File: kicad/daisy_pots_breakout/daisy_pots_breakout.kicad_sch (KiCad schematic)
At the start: 6 parts, among them J1 Conn_01x11_Pin, SW1 RotaryEncoder_Switch

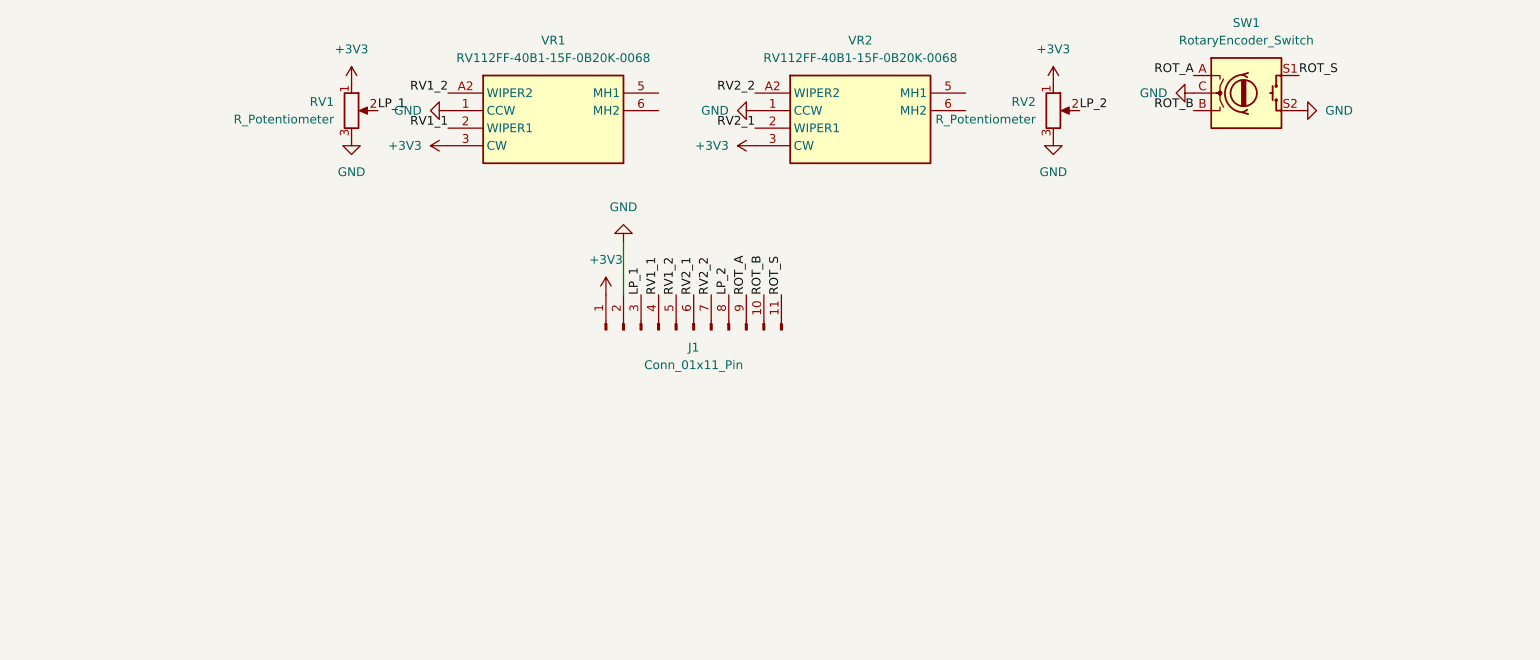
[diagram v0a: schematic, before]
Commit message: Make side boards for pots and buttons use same connector as main board
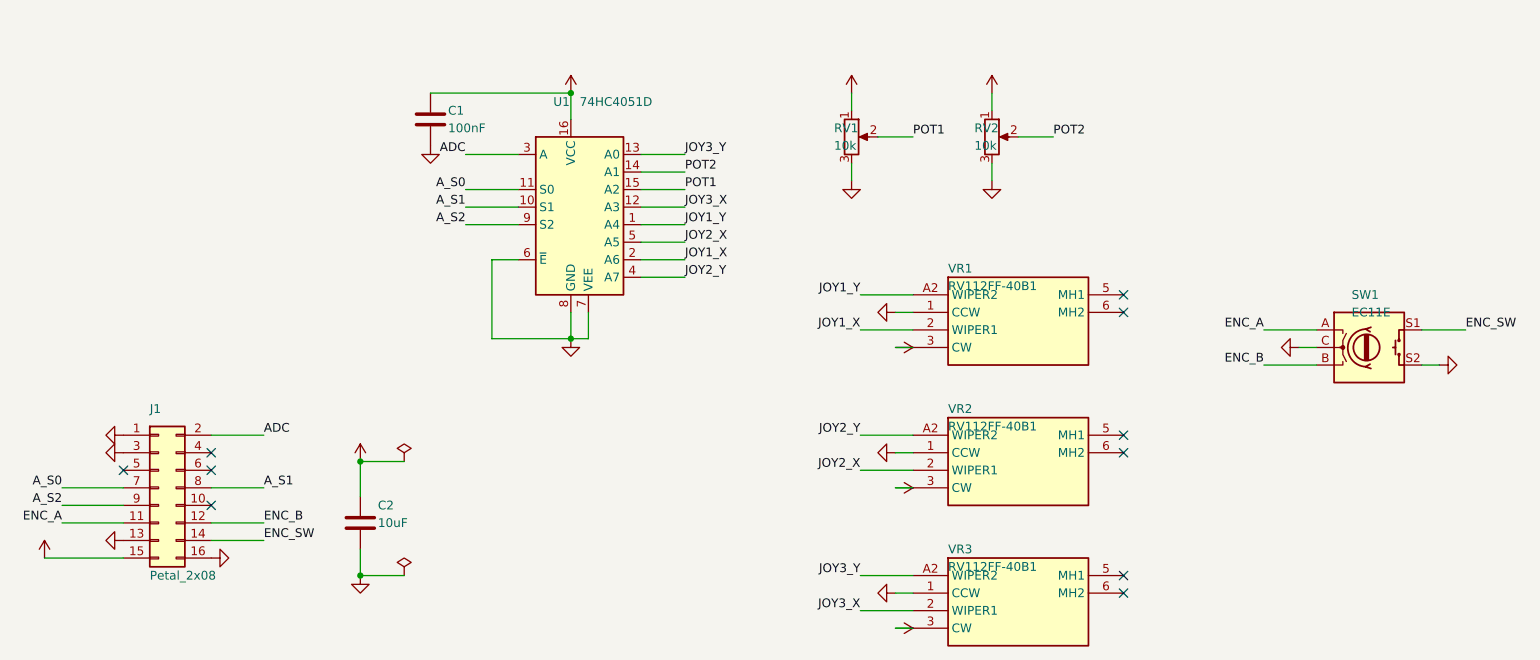
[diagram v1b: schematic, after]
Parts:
- removed J1: Conn_01x11_Pin, Connector_PinHeader_2.54mm:PinHeader_1x11_P2.54mm_Vertical, symbol Connector:Conn_01x11_Pin
- added C1: 100nF, Capacitor_SMD:C_0603_1608Metric_Pad1.08x0.95mm_HandSolder, symbol Device:C
- added C2: 10uF, Capacitor_SMD:C_0603_1608Metric_Pad1.08x0.95mm_HandSolder, symbol Device:C
- added J1: Petal_2x08, Connector_PinSocket_2.54mm:PinSocket_2x08_P2.54mm_Horizontal, symbol Connector_Generic:Conn_02x08_Odd_Even
- added U1: 74HC4051D, Package_SO:SOIC-16_3.9x9.9mm_P1.27mm, symbol 74xx:74HC4051
- added VR3: RV112FF-40B1, RV112FF:RV112FF40B115F0B20K0068, symbol RV112FF:RV112FF-40B1-15F-0B20K-0068
- RV1, RV2: value R_Potentiometer -> 10k
- SW1: value RotaryEncoder_Switch -> EC11E
- VR1, VR2: value RV112FF-40B1-15F-0B20K-0068 -> RV112FF-40B1; Height 25 -> (none); Manufacturer_Name Alpha (Taiwan) -> (none); Manufacturer_Part_Number RV112FF-40B1-15F-0B20K-0068 -> (none); Mouser Part Number 317-1240FF-15F-0B20K -> (none); Mouser Price/Stock https://www.mouser.co.uk/ProductDetail/Alpha-Taiwan/RV112FF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 -> (none)
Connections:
- net GND: now also C1.2, C2.2, J1.1 (Pin_1), J1.13 (Pin_13), J1.16 (Pin_16), J1.3 (Pin_3), U1.6 (~{E}), U1.7 (VEE), U1.8 (GND), VR3.1 (CCW)
- net +3V3 renamed +3.3VA
- net +3.3VA: now also C1.1, C2.1, J1.15 (Pin_15), U1.16 (VCC), VR3.3 (CW)
- net LP_1 renamed POT1
- net POT1: now also U1.15 (A2)
- net LP_2 renamed POT2
- net POT2: now also U1.14 (A1)
- net ROT_A renamed ENC_A
- net ENC_A: now also J1.11 (Pin_11)
- net ROT_B renamed ENC_B
- net ENC_B: now also J1.12 (Pin_12)
- net ROT_S renamed ENC_SW
- net ENC_SW: now also J1.14 (Pin_14)
- net RV1_1 renamed JOY1_X
- net JOY1_X: now also U1.2 (A6)
- net RV1_2 renamed JOY1_Y
- net JOY1_Y: now also U1.1 (A4)
- net RV2_1 renamed JOY2_X
- net JOY2_X: now also U1.5 (A5)
- net RV2_2 renamed JOY2_Y
- net JOY2_Y: now also U1.4 (A7)
- new net ADC: J1.2 (Pin_2), U1.3 (A)
- new net A_S0: J1.7 (Pin_7), U1.11 (S0)
- new net A_S1: J1.8 (Pin_8), U1.10 (S1)
- new net A_S2: J1.9 (Pin_9), U1.9 (S2)
- new net JOY3_X: U1.12 (A3), VR3.2 (WIPER1)
- new net JOY3_Y: U1.13 (A0), VR3.A2 (WIPER2)
- no-connect marks 0 -> 10
